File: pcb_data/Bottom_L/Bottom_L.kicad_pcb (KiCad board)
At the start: 2 copper layers, 158.4 x 96.4 mm, 85 parts, among them J1 Conn_01x02, U1 XIAO-nRF52840

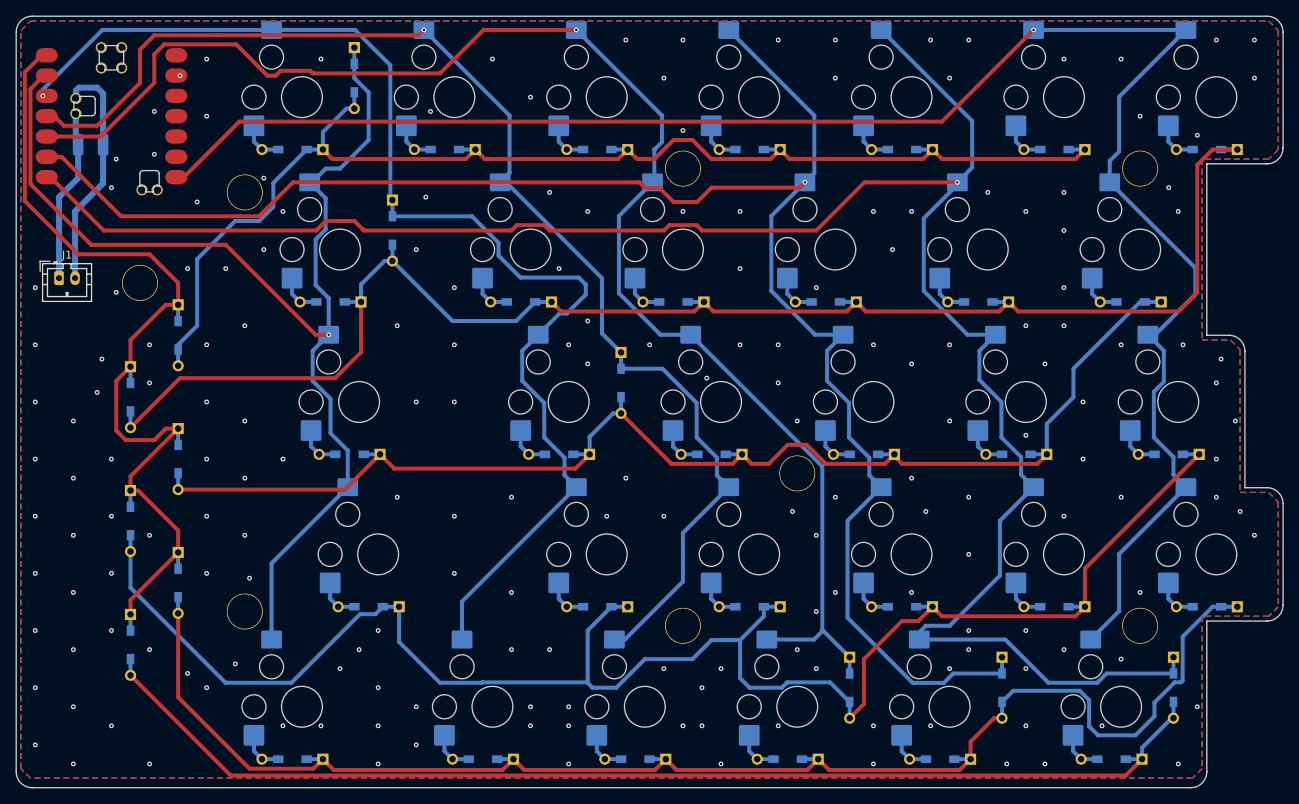
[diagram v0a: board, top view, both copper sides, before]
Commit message: remove unnecessary footprint
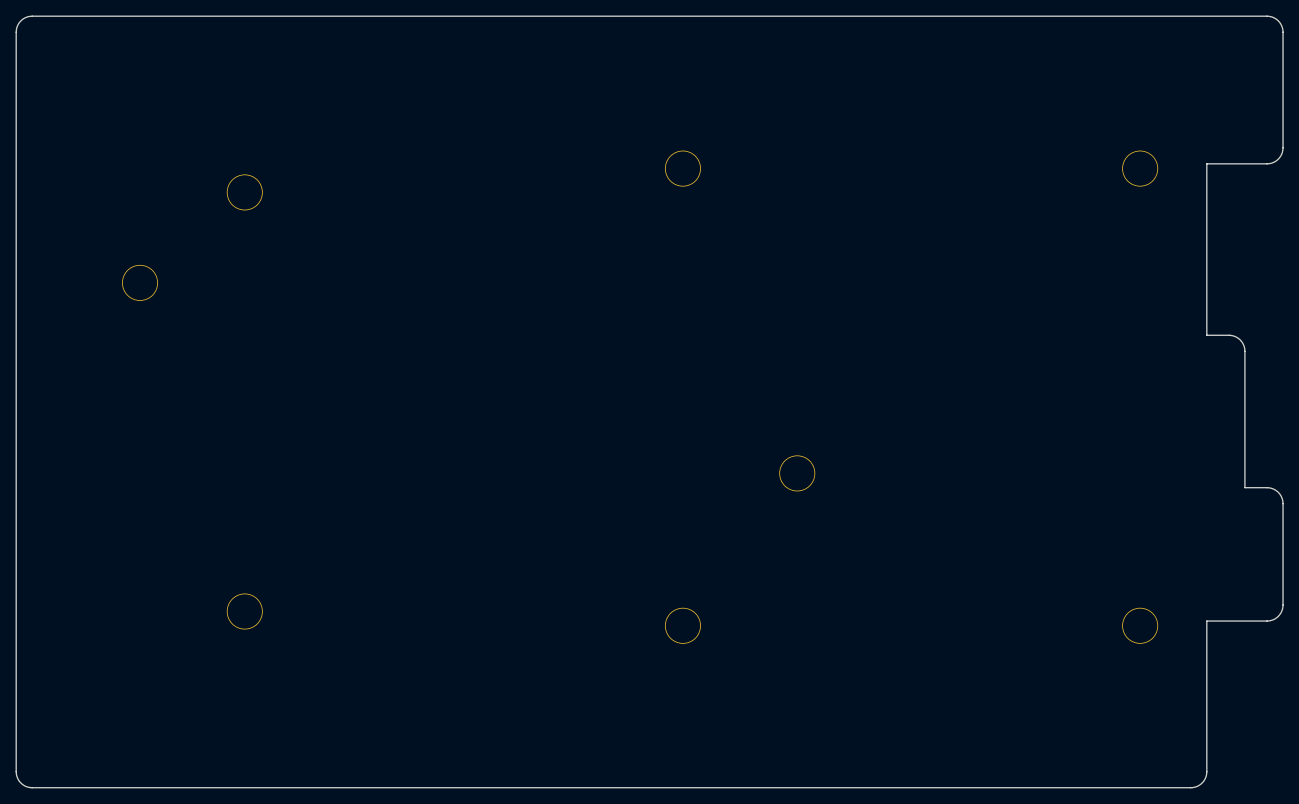
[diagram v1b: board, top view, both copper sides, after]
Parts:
- removed C1: GRM32EC81C476KE15L, Capacitor_SMD:C_1210_3225Metric_Pad1.33x2.70mm_HandSolder
- removed D0-1, D0-2, D0-3, D0-4, D1-0, D1-2, D1-3, D1-4, D2-0, D2-1, D2-3, D2-4, D3-0, D3-1, D3-2, D3-4, D4-0, D4-1, D4-2, D4-3, D5-0, D5-1, D5-2, D5-3, D5-4, D6-0, D6-1, D6-2, D6-3, D6-4, D6-5, DI0, DI1, DI2, DI3, DI4, DI5, DS0, DS1, DS2, DS3, DS4, DS5: 1N4148W, kbd_Parts:Diode_TH_SMD
- removed J1: Conn_01x02, Connector_JST:JST_PH_B2B-PH-K_1x02_P2.00mm_Vertical
- removed RC0-1: SW_Push, custom-library:Kailh-PG1353-Hotswap-L-1.5U
- removed RC0-2: SW_Push, custom-library:Kailh-PG1353-Hotswap-L-1.75U
- removed RC0-3: SW_Push, custom-library:Kailh-PG1353-Hotswap-L-2U
- removed RC0-4, RC1-0, RC1-2, RC1-3, RC1-4, RC2-0, RC2-1, RC2-3, RC2-4, RC3-0, RC3-1, RC3-2, RC3-4, RC4-0, RC4-1, RC4-2, RC4-3, RC5-0, RC5-1, RC5-2, RC5-3, RC5-4, RC6-0, RC6-1, RC6-2, RC6-3, RC6-4: SW_Push, custom-library:Kailh-PG1353-Hotswap-L-1U
- removed RC6-5: SW_Push, custom-library:Kailh-PG1353-Hotswap-L-1.25U
- removed U1: XIAO-nRF52840, mcu:xiao-ble-smd-cutout
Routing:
- net IO 5: track 257.7 -> 0.00 mm, vias 1 -> 0
- net IO 6: track 229.0 -> 0.00 mm, vias 1 -> 0
- net IO 4: track 217.6 -> 0.00 mm, vias 1 -> 0
- net Net-(D0-3-K): track 214.1 -> 0.00 mm
- net Net-(D0-1-K): track 191.5 -> 0.00 mm
- net IO 3: track 186.5 -> 0.00 mm, vias 1 -> 0
- net Net-(D0-4-K): track 185.1 -> 0.00 mm
- net Net-(D0-2-K): track 163.2 -> 0.00 mm
- net IO 2: track 159.4 -> 0.00 mm, vias 1 -> 0
- net Net-(D1-0-K): track 159.2 -> 0.00 mm
- net IO 1: track 153.7 -> 0.00 mm, vias 1 -> 0
- net IO 0: track 147.0 -> 0.00 mm, vias 1 -> 0
- net Net-(D6-5-K): track 145.5 -> 0.00 mm
- net INTR_L: track 118.4 -> 0.00 mm
- net GND: track 29.4 -> 0.00 mm, vias 192 -> 0
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- removed copper zone on B.Cu, net GND
- removed copper zone on F.Cu, net GND

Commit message: fix hole footprint and number
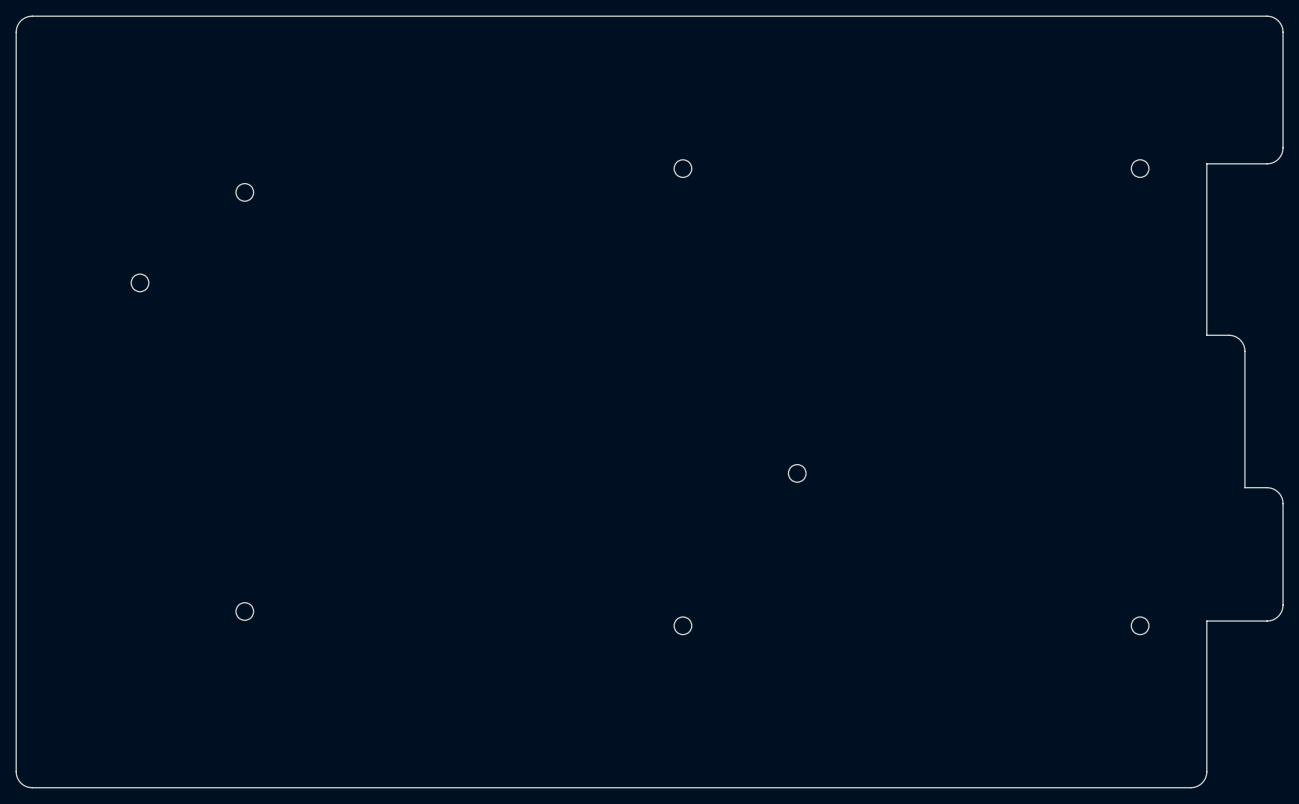
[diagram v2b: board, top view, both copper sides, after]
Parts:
- H1, H2, H3, H4, H5, H6: footprint kbd_Hole:m2_Spacer_Hole -> kbd_Hole:m2_Screw_Hole
- H7: renamed from H8; footprint kbd_Hole:m2_Spacer_Hole -> kbd_Hole:m2_Screw_Hole
- H8: renamed from H7; footprint kbd_Hole:m2_Spacer_Hole -> kbd_Hole:m2_Screw_Hole
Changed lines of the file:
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@@
 	)
 	(net 0 "")
-	(footprint "kbd_Hole:m2_Spacer_Hole"
+	(footprint "kbd_Hole:m2_Screw_Hole"
 		(layer "F.Cu")
 		(at 185.737656 66.079743)
@@
 			)
 		)
-		(property "Datasheet" "~"
-			(at 0 0 0)
-			(layer "F.Fab")
-			(hide yes)
-			(effects
-				(font
-					(size 1.27 1.27)
-					(thickness 0.15)
-				)
-			)
-		)
-		(property "Description" "Mounting Hole without connection"
+		(property "Datasheet" ""
+			(at 0 0 0)
+			(layer "F.Fab")
+			(hide yes)
+			(effects
+				(font
+					(size 1.27 1.27)
+					(thickness 0.15)
+				)
+			)
+		)
+		(property "Description" ""
 			(at 0 0 0)
 			(layer "F.Fab")
@@
 		(fp_circle
 			(center 0 0)
-			(end 2.3 0)
+			(end 2.45 0)
 			(stroke
 				(width 0.05)
@@
 		(pad "" np_thru_hole circle
 			(at 0 0)
-			(size 4.5 4.5)
-			(drill 4.3)
+			(size 2.2 2.2)
+			(drill 2.2)
 			(layers "*.Cu" "*.Mask")
 		)
 		(embedded_fonts no)
 	)
-	(footprint "kbd_Hole:m2_Spacer_Hole"
+	(footprint "kbd_Hole:m2_Screw_Hole"
 		(layer "F.Cu")
 		(at 60.721926 80.367255)
 		(descr "Mounting Hole 2.2mm, no annular, M2")
 		(tags "mounting hole 2.2mm no annular m2")
-		(property "Reference" "H7"
+		(property "Reference" "H8"
 			(at 0 -3.2 0)
 			(layer "F.Fab")
@@
 			)
 		)
-		(property "Datasheet" "~"
-			(at 0 0 0)
-			(layer "F.Fab")
-			(hide yes)
-			(effects
-				(font
-					(size 1.27 1.27)
-					(thickness 0.15)
-				)
-			)
-		)
-		(property "Description" "Mounting Hole without connection"
+		(property "Datasheet" ""
+			(at 0 0 0)
+			(layer "F.Fab")
+			(hide yes)
+			(effects
+				(font
+					(size 1.27 1.27)
+					(thickness 0.15)
+				)
+			)
+		)
+		(property "Description" ""
 			(at 0 0 0)
 			(layer "F.Fab")
@@
 		(fp_circle
 			(center 0 0)
-			(end 2.3 0)
+			(end 2.45 0)
 			(stroke
 				(width 0.05)
@@
 		(pad "" np_thru_hole circle
 			(at 0 0)
-			(size 4.5 4.5)
-			(drill 4.3)
+			(size 2.2 2.2)
+			(drill 2.2)
 			(layers "*.Cu" "*.Mask")
 		)
 		(embedded_fonts no)
 	)
-	(footprint "kbd_Hole:m2_Spacer_Hole"
+	(footprint "kbd_Hole:m2_Screw_Hole"
 		(layer "F.Cu")
 		(at 185.737656 123.229791)
@@
 			)
 		)
-		(property "Datasheet" "~"
-			(at 0 0 0)
-			(layer "F.Fab")
-			(hide yes)
-			(effects
-				(font
-					(size 1.27 1.27)
-					(thickness 0.15)
-				)
-			)
-		)
-		(property "Description" "Mounting Hole without connection"
+		(property "Datasheet" ""
+			(at 0 0 0)
+			(layer "F.Fab")
+			(hide yes)
+			(effects
+				(font
+					(size 1.27 1.27)
+					(thickness 0.15)
+				)
+			)
+		)
+		(property "Description" ""
 			(at 0 0 0)
 			(layer "F.Fab")
@@
 		(fp_circle
 			(center 0 0)
-			(end 2.3 0)
+			(end 2.45 0)
 			(stroke
 				(width 0.05)
@@
 		(pad "" np_thru_hole circle
 			(at 0 0)
-			(size 4.5 4.5)
-			(drill 4.3)
+			(size 2.2 2.2)
+			(drill 2.2)
 			(layers "*.Cu" "*.Mask")
 		)
 		(embedded_fonts no)
 	)
-	(footprint "kbd_Hole:m2_Spacer_Hole"
+	(footprint "kbd_Hole:m2_Screw_Hole"
 		(layer "F.Cu")
 		(at 73.818812 69.056308)
@@
 			)
 		)
-		(property "Datasheet" "~"
-			(at 0 0 0)
-			(layer "F.Fab")
-			(hide yes)
-			(effects
-				(font
-					(size 1.27 1.27)
-					(thickness 0.15)
-				)
-			)
-		)
-		(property "Description" "Mounting Hole without connection"
+		(property "Datasheet" ""
+			(at 0 0 0)
+			(layer "F.Fab")
+			(hide yes)
+			(effects
+				(font
+					(size 1.27 1.27)
+					(thickness 0.15)
+				)
+			)
+		)
+		(property "Description" ""
 			(at 0 0 0)
 			(layer "F.Fab")
@@
 		(fp_circle
 			(center 0 0)
-			(end 2.3 0)
+			(end 2.45 0)
 			(stroke
 				(width 0.05)
@@
 		(pad "" np_thru_hole circle
 			(at 0 0)
-			(size 4.5 4.5)
-			(drill 4.3)
+			(size 2.2 2.2)
+			(drill 2.2)
 			(layers "*.Cu" "*.Mask")
 		)
 		(embedded_fonts no)
 	)
-	(footprint "kbd_Hole:m2_Spacer_Hole"
+	(footprint "kbd_Hole:m2_Screw_Hole"
 		(layer "F.Cu")
 		(at 128.587608 123.229791)
@@
 			)
 		)
-		(property "Datasheet" "~"
-			(at 0 0 0)
-			(layer "F.Fab")
-			(hide yes)
-			(effects
-				(font
-					(size 1.27 1.27)
-					(thickness 0.15)
-				)
-			)
-		)
-		(property "Description" "Mounting Hole without connection"
+		(property "Datasheet" ""
+			(at 0 0 0)
+			(layer "F.Fab")
+			(hide yes)
+			(effects
+				(font
+					(size 1.27 1.27)
+					(thickness 0.15)
+				)
+			)
+		)
+		(property "Description" ""
 			(at 0 0 0)
 			(layer "F.Fab")
@@
 		(fp_circle
 			(center 0 0)
-			(end 2.3 0)
+			(end 2.45 0)
 			(stroke
 				(width 0.05)
@@
 		(pad "" np_thru_hole circle
 			(at 0 0)
-			(size 4.5 4.5)
-			(drill 4.3)
+			(size 2.2 2.2)
+			(drill 2.2)
 			(layers "*.Cu" "*.Mask")
 		)
 		(embedded_fonts no)
 	)
-	(footprint "kbd_Hole:m2_Spacer_Hole"
+	(footprint "kbd_Hole:m2_Screw_Hole"
 		(layer "F.Cu")
 		(at 142.87512 104.179775)
 		(descr "Mounting Hole 2.2mm, no annular, M2")
 		(tags "mounting hole 2.2mm no annular m2")
-		(property "Reference" "H8"
+		(property "Reference" "H7"
 			(at 0 -3.2 0)
 			(layer "F.Fab")
@@
 			)
 		)
-		(property "Datasheet" "~"
-			(at 0 0 0)
-			(layer "F.Fab")
-			(hide yes)
-			(effects
-				(font
-					(size 1.27 1.27)
-					(thickness 0.15)
-				)
-			)
-		)
-		(property "Description" "Mounting Hole without connection"
+		(property "Datasheet" ""
+			(at 0 0 0)
+			(layer "F.Fab")
+			(hide yes)
+			(effects
+				(font
+					(size 1.27 1.27)
+					(thickness 0.15)
+				)
+			)
+		)
+		(property "Description" ""
 			(at 0 0 0)
 			(layer "F.Fab")
@@
 		(fp_circle
 			(center 0 0)
-			(end 2.3 0)
+			(end 2.45 0)
 			(stroke
 				(width 0.05)
@@
 		(pad "" np_thru_hole circle
 			(at 0 0)
-			(size 4.5 4.5)
-			(drill 4.3)
+			(size 2.2 2.2)
+			(drill 2.2)
 			(layers "*.Cu" "*.Mask")
 		)
 		(embedded_fonts no)
 	)
-	(footprint "kbd_Hole:m2_Spacer_Hole"
+	(footprint "kbd_Hole:m2_Screw_Hole"
 		(layer "F.Cu")
 		(at 128.587608 66.079743)
@@
 			)
 		)
-		(property "Datasheet" "~"
-			(at 0 0 0)
-			(layer "F.Fab")
-			(hide yes)
-			(effects
-				(font
-					(size 1.27 1.27)
-					(thickness 0.15)
-				)
-			)
-		)
-		(property "Description" "Mounting Hole without connection"
+		(property "Datasheet" ""
+			(at 0 0 0)
+			(layer "F.Fab")
+			(hide yes)
+			(effects
+				(font
+					(size 1.27 1.27)
+					(thickness 0.15)
+				)
+			)
+		)
+		(property "Description" ""
 			(at 0 0 0)
 			(layer "F.Fab")
@@
 		(fp_circle
 			(center 0 0)
-			(end 2.3 0)
+			(end 2.45 0)
 			(stroke
 				(width 0.05)
@@
 		(pad "" np_thru_hole circle
 			(at 0 0)
-			(size 4.5 4.5)
-			(drill 4.3)
+			(size 2.2 2.2)
+			(drill 2.2)
 			(layers "*.Cu" "*.Mask")
 		)
 		(embedded_fonts no)
 	)
-	(footprint "kbd_Hole:m2_Spacer_Hole"
+	(footprint "kbd_Hole:m2_Screw_Hole"
 		(layer "F.Cu")
 		(at 73.818812 121.443852)
@@
 			)
 		)
-		(property "Datasheet" "~"
-			(at 0 0 0)
-			(layer "F.Fab")
-			(hide yes)
-			(effects
-				(font
-					(size 1.27 1.27)
-					(thickness 0.15)
-				)
-			)
-		)
-		(property "Description" "Mounting Hole without connection"
+		(property "Datasheet" ""
+			(at 0 0 0)
+			(layer "F.Fab")
+			(hide yes)
+			(effects
+				(font
+					(size 1.27 1.27)
+					(thickness 0.15)
+				)
+			)
+		)
+		(property "Description" ""
 			(at 0 0 0)
 			(layer "F.Fab")
@@
 		(fp_circle
 			(center 0 0)
-			(end 2.3 0)
+			(end 2.45 0)
 			(stroke
 				(width 0.05)
@@
 		(pad "" np_thru_hole circle
 			(at 0 0)
-			(size 4.5 4.5)
-			(drill 4.3)
+			(size 2.2 2.2)
+			(drill 2.2)
 			(layers "*.Cu" "*.Mask")
 		)
